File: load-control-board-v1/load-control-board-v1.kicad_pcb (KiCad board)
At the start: 4 copper layers, 100 x 80 mm, 79 parts, among them CN1 3511232BMRS0BNA2, Q1 AO3400A, Q2 AO3400A, Q3 IRFP7530PBF, U1 LM317_SOT-223, U10 OPA188xxDBV, U11 OPA188xxDBV, U12 INA186A1IDCKR, U2 74AHC1G04, U22 TL081HIDBVR, U22 TL081HIDR, U3 LM317_SOT-223, U4 TT56145145-1520, U5 REF5025AD, U6 SN74LVC1G123DCUR_C352969, U7 TL081HIDBVR, U8 OPA188xxDBV, U9 TT56145145-1520

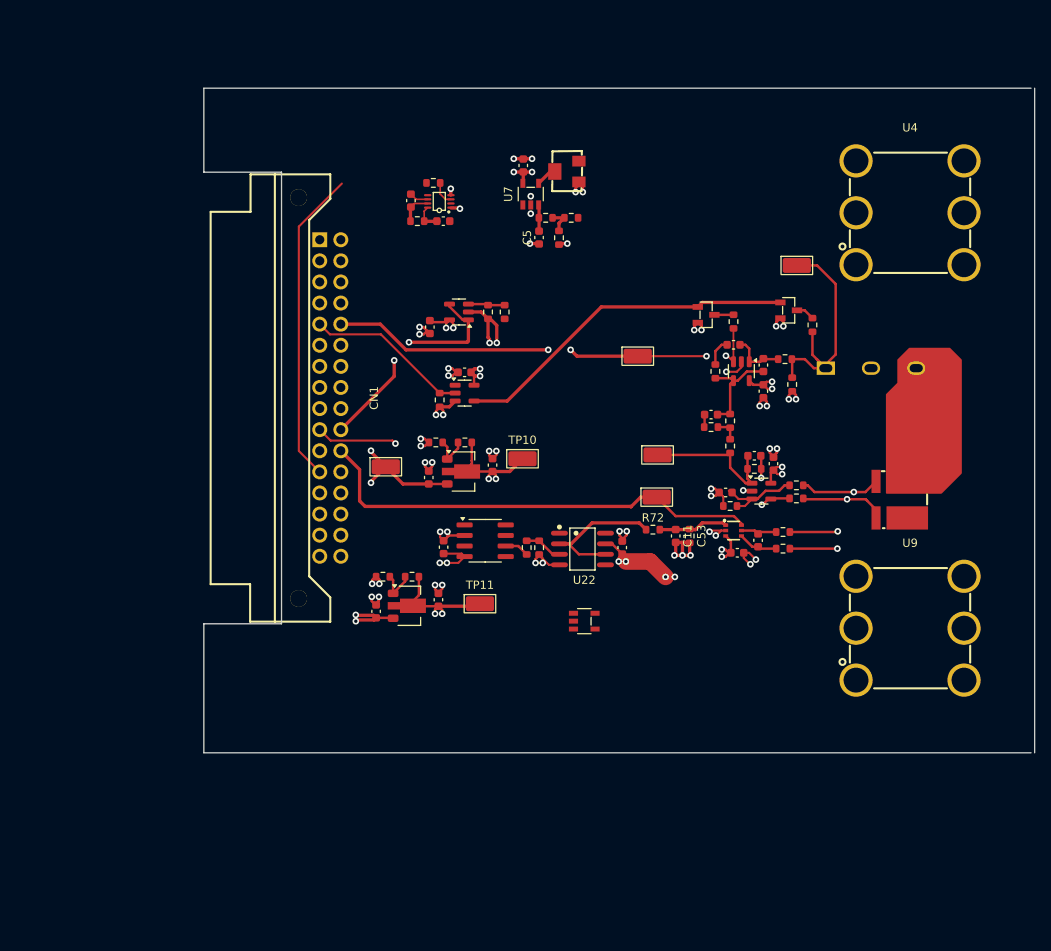
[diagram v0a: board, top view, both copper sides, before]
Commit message: Change layout of LDO and VBUS monitor
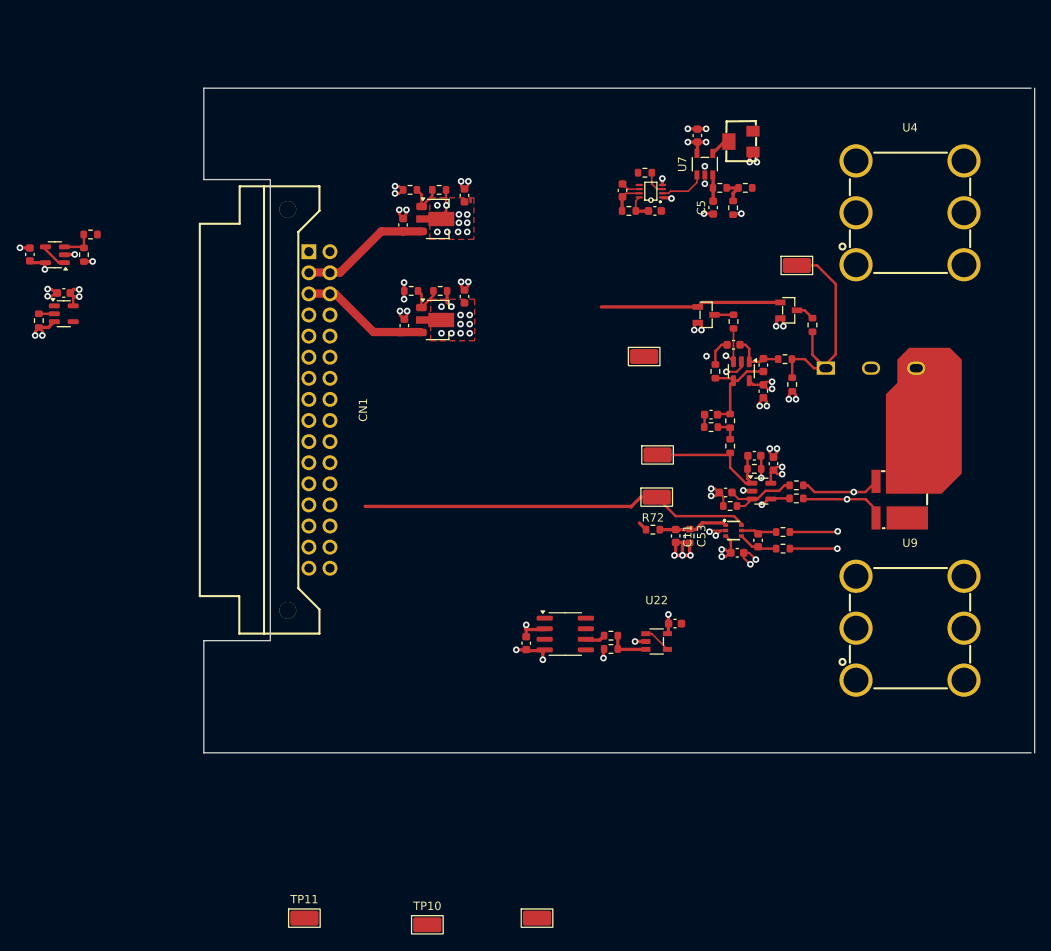
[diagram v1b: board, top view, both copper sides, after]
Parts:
- removed the U22 at (99.8, 109.3)
- moved TP1 57.3 mm to (94.4, 153.7)
- moved TP10 57.3 mm to (81.2, 154.5)
- moved R14 50.7 mm to (40.6, 71.4), turned to 180 degrees
- moved C2 49.2 mm to (37.4, 78.4)
- moved R1 49.2 mm to (34.4, 81.8)
- moved U2 49.2 mm to (37.4, 80.9)
- moved R15 49.1 mm to (39.8, 73.8)
- moved U8 49.1 mm to (36.3, 73.8)
- moved C12 48.9 mm to (33.3, 73.8), turned to -90 degrees
- moved TP11 43.3 mm to (66.4, 153.7)
- moved C6 36.6 mm to (85.6, 78.9)
- moved R6 34.6 mm to (82.7, 78.2)
- moved R7 34.6 mm to (79.2, 78.2)
- moved U3 34.6 mm to (82.4, 81.7)
- moved C4 34.6 mm to (78.4, 82.4)
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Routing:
- net I_CONTROL: track 53.3 -> 7.58 mm, vias 4 -> 2
- net OV_ALERT: track 37.9 -> 0.00 mm
- net +5V: track 69.3 -> 31.6 mm, vias 17 -> 19
- net V_BUS_MON: track 26.9 -> 3.24 mm, vias 2 -> 0
- net ~{ENABLE}: track 41.8 -> 21.8 mm
- net ENABLE: track 19.7 -> 1.86 mm
- net GND: track 86.6 -> 72.0 mm, vias 57 -> 54
- net +9V: track 27.0 -> 12.5 mm, vias 6 -> 14
- net V_REF: track 17.9 -> 4.54 mm
- net +12V: track 20.8 -> 30.9 mm, vias 4 -> 0
- net /I_SINK_MON_CH0: track 55.2 -> 47.3 mm
- net Net-(U6-B): track 0.00 -> 5.58 mm
- net Net-(U5-Vout): track 2.95 -> 2.42 mm
- added copper zone on F.Cu, net +9V
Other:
- outline, holes or cut-outs redrawn

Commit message: Add filled zone for mosfet, change terminal to from THO to SMT
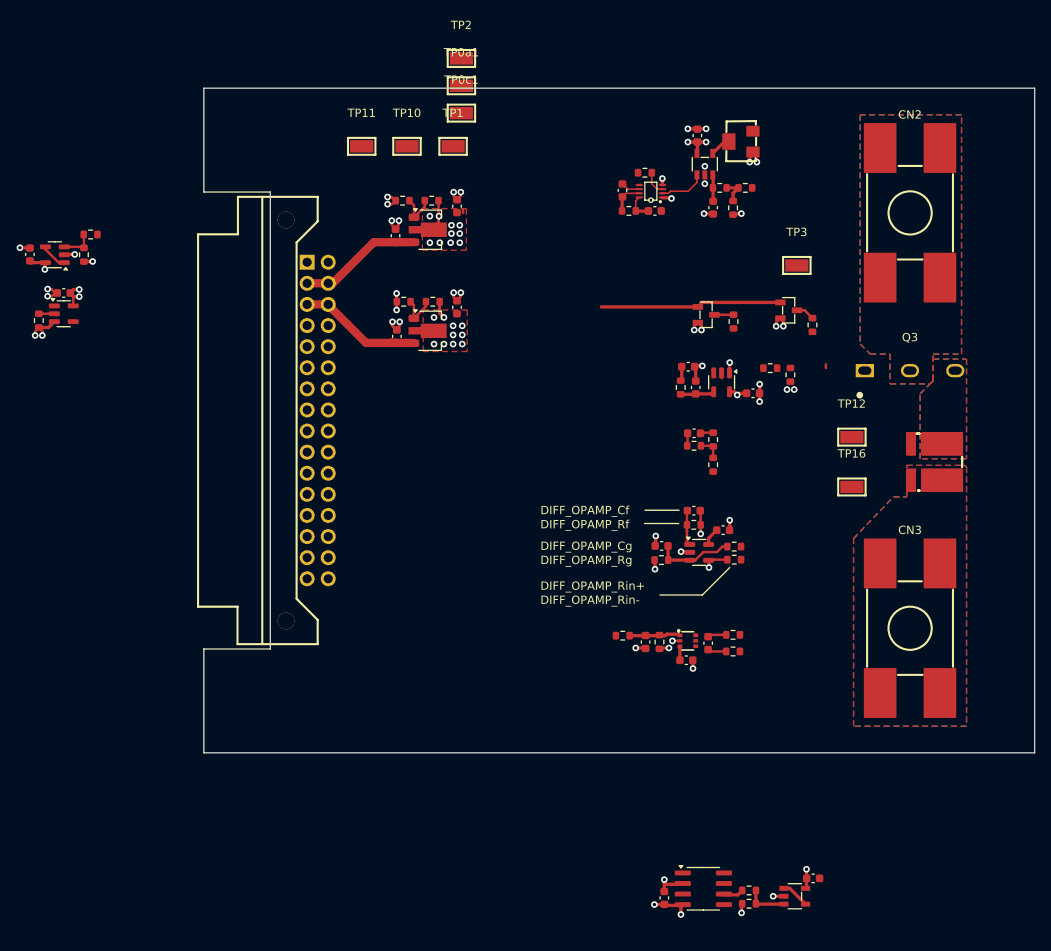
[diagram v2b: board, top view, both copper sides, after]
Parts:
- removed U4, U9: TT56145145-1520, programmable-load-library:TH_6P-TT56145145-1500
- added CN2: BTC22M4NBB4SCM, programmable-load-library:CONN-SMD_L10.8-W10.0-LS17.4, F.Cu at (139.3, 68.8)
- added CN3: BTC22M4NBB4SCM, programmable-load-library:CONN-SMD_L10.8-W10.0-LS17.4, F.Cu at (139.3, 118.8)
- added R_SHUNT1: BVB-M-R001-1.0, programmable-load-library:RES-SMD_4P-L6.9-W6.6_SBB-K-2F-N-T5, F.Cu at (141.3, 98.8)
- added TP12: V_SHUNT_P, programmable-load-library:SMD_RH-5015, F.Cu at (132.3, 95.8)
- added TP16: V_SHUNT_N, programmable-load-library:SMD_RH-5015, F.Cu at (132.3, 101.8)
- Q3: footprint programmable-load-library:PG-TO247-3_L15.9-W5.2-P5.44-L -> programmable-load-library:PG-TO247-3_L15.9-W5.2-P5.44-L_1_Horizontal; moved to F.Cu
- TP0a1: value TestPoint -> I_SINK_MON; footprint TestPoint:TestPoint_Keystone_5015_Micro_Mini -> programmable-load-library:SMD_RH-5015
- TP0c1: value TestPoint -> I_CONTROL_IN; footprint TestPoint:TestPoint_Keystone_5015_Micro_Mini -> programmable-load-library:SMD_RH-5015
- TP1, TP10, TP11: footprint TestPoint:TestPoint_Keystone_5015_Micro_Mini -> programmable-load-library:SMD_RH-5015
- TP2: value TestPoint -> DIFF_OUT; footprint TestPoint:TestPoint_Keystone_5015_Micro_Mini -> programmable-load-library:SMD_RH-5015
- TP3: value TestPoint -> MOS_G; footprint TestPoint:TestPoint_Keystone_5015_Micro_Mini -> programmable-load-library:SMD_RH-5015
- moved TP10 93.7 mm to (78.7, 60.8)
- moved TP1 93.4 mm to (84.3, 60.8)
- moved TP11 93.2 mm to (73.3, 60.8)
- moved TP0a1 54.8 mm to (85.3, 53.5)
- moved TP2 53.2 mm to (85.3, 50.2)
- moved TP0c1 36.6 mm to (85.3, 56.8)
- moved C49 34.9 mm to (127.6, 148.9)
- moved C8 34.9 mm to (109.7, 151.3)
- moved R11 34.9 mm to (119.9, 150.4)
- moved U5 34.9 mm to (114.4, 150.2)
- moved R12 34.9 mm to (119.9, 152.0)
- moved U22 34.9 mm to (125.4, 151.1)
- moved U12 14.4 mm to (112.5, 120.3)
- moved C21 14.3 mm to (112.3, 122.7)
- moved C20 13.8 mm to (115.0, 120.6)
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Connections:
- R_SHUNT1 pad 2: GND -> GNDPWR
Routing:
- net /I_SINK_MON_CH0: track 47.3 -> 0.18 mm
- net /ch0/MOS_G: track 29.6 -> 0.47 mm
- net /ch0/V_Rs0p: track 23.1 -> 0.07 mm, vias 2 -> 0
- net /ch0/V_Rs0n: track 20.5 -> 0.00 mm, vias 2 -> 0
- net GND: track 72.0 -> 54.5 mm, vias 54 -> 49
- net Net-(C15-Pad1): track 17.6 -> 4.17 mm
- net I_CONTROL: track 7.58 -> 0.01 mm, vias 2 -> 0
- net Net-(U11--): track 12.1 -> 5.65 mm
- net Net-(U10--): track 6.40 -> 10.7 mm
- net +9V: track 12.5 -> 8.42 mm, vias 14 -> 11
- net +5V: track 31.6 -> 28.8 mm, vias 19 -> 17
- net Net-(U12-IN+): track 4.81 -> 2.27 mm
- net /ch0/V_REF_FIL: track 8.38 -> 6.19 mm
- net Net-(U12-IN-): track 4.43 -> 2.27 mm
- net Net-(U10-+): track 10.1 -> 8.53 mm
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- added copper zone on F.Cu, net +5V
- added copper zone on B.Cu, net GNDPWR
- added copper zone on F.Cu, net GNDPWR
- added copper zone on B.Cu, net Net-(Q3-S)
- added copper zone on F.Cu, net Net-(Q3-S)
- added copper zone on B.Cu, net VBUS
- added copper zone on F.Cu, net VBUS
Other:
- outline, holes or cut-outs redrawn
- board text added: "0.25V Reference voltage block"
- board text added: "DIFF_OPAMP_Cf"
- board text added: "DIFF_OPAMP_Cg"
- board text added: "DIFF_OPAMP_Rf"
- board text added: "DIFF_OPAMP_Rg"
- board text added: "DIFF_OPAMP_Rin+"
- board text added: "DIFF_OPAMP_Rin-"
- board text added: "INA186 shunt voltage amp & Reference LPF"
- board text added: "Negative feedback Op-Amp"
- board text added: "Shunt voltage DIfferential Op-Amp"

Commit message: Complete second times layout (no copper filled)
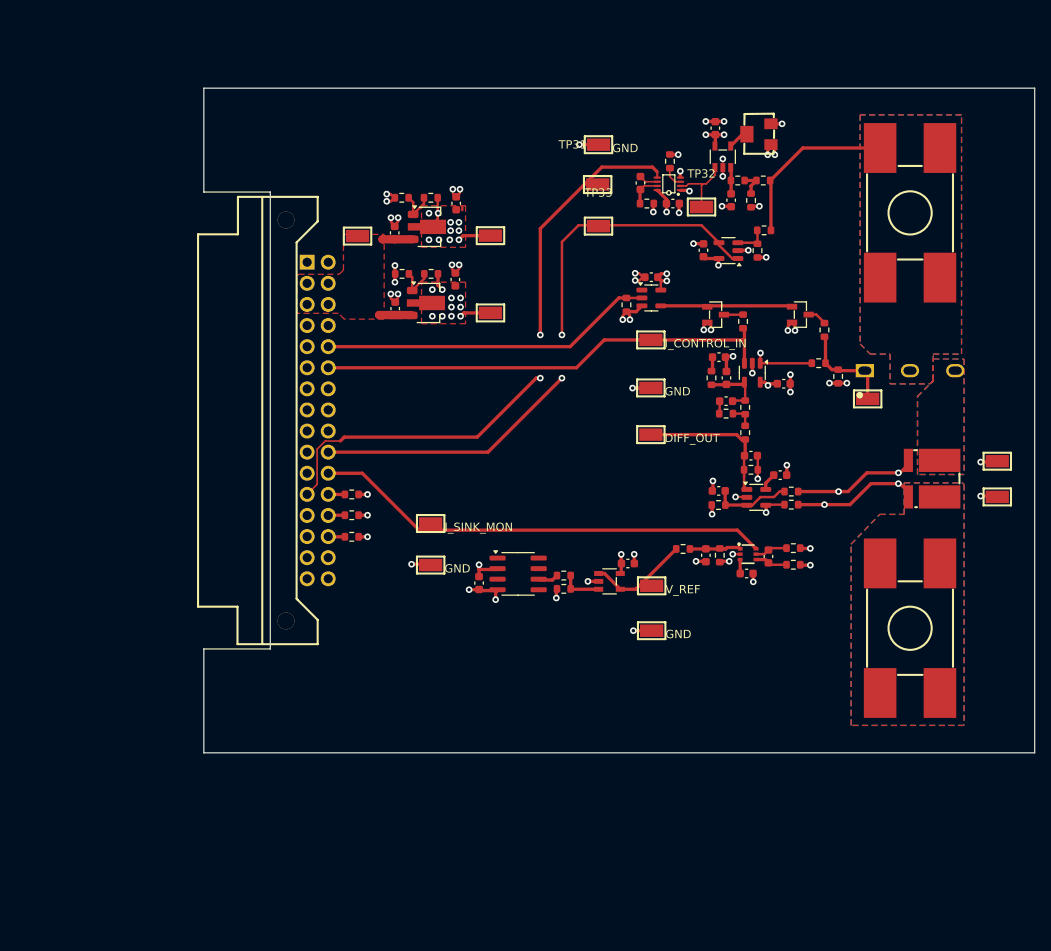
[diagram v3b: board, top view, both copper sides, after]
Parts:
- removed the R_SHUNT1 at (141.3, 98.8) (x2)
- added R76: 10k, Resistor_SMD:R_0603_1608Metric, F.Cu at (72.1, 102.7)
- added R77: 10k, Resistor_SMD:R_0603_1608Metric, F.Cu at (72.1, 105.2)
- added R78: 10k, Resistor_SMD:R_0603_1608Metric, F.Cu at (72.1, 107.8)
- added R_SHUNT1: BVB-M-R001-1.0, programmable-load-library:RES-SMD_4P-L6.9-W6.6_SBB-K-2F-N-T5, F.Cu at (140.9, 100.8)
- added TP20: GND, programmable-load-library:SMD_RH-5015, F.Cu at (101.8, 60.6)
- added TP21: GND, programmable-load-library:SMD_RH-5015, F.Cu at (108.2, 119.1)
- added TP22: GND, programmable-load-library:SMD_RH-5015, F.Cu at (81.6, 111.2)
- added TP26: GND, programmable-load-library:SMD_RH-5015, F.Cu at (108.1, 89.9)
- added TP30: REF, programmable-load-library:SMD_RH-5015, F.Cu at (108.2, 113.7)
- added TP31: V_BUS_MON, programmable-load-library:SMD_RH-5015, F.Cu at (101.7, 65.4)
- added TP32: VBUS_COMP_OUT, programmable-load-library:SMD_RH-5015, F.Cu at (114.2, 68.1)
- added TP33: OV_ALERT, programmable-load-library:SMD_RH-5015, F.Cu at (101.8, 70.4)
- U7: value TL081HIDBVR -> ALERT_COMP_OUT
- moved C12 81.1 mm to (114.4, 73.3)
- moved R14 81.1 mm to (121.7, 70.9)
- moved R15 81.1 mm to (120.9, 73.3)
- moved U8 81.1 mm to (117.4, 73.3)
- moved C2 70.8 mm to (108.1, 76.5)
- moved R1 70.8 mm to (105.1, 79.9)
- moved U2 70.8 mm to (108.1, 79.0)
- moved TP0a1 52.8 mm to (81.6, 106.2)
- moved TP2 50.7 mm to (108.1, 95.5)
- moved C49 44.0 mm to (105.3, 111.0)
- moved C8 44.0 mm to (87.4, 113.4)
- moved R11 44.0 mm to (97.6, 112.5)
- moved U5 44.0 mm to (92.1, 112.3)
- moved R12 44.0 mm to (97.6, 114.1)
- moved U22 44.0 mm to (103.1, 113.2)
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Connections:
- CN1 pad 21: I_CONTROL -> ENABLE
- CN1 pad 22: unconnected-(CN1-B6-Pad22) -> I_CONTROL
- CN1 pad 5: ENABLE -> unconnected-(CN1-A5-Pad5)
- R10 pad 1: 5V -> +5V
- R9 pad 3: 5V -> +5V
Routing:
- net OV_ALERT: track 0.00 -> 72.4 mm, vias 0 -> 2
- net V_BUS_MON: track 3.24 -> 72.1 mm, vias 0 -> 2
- net I_CONTROL: track 0.01 -> 55.8 mm
- net /I_SINK_MON_CH0: track 0.18 -> 55.4 mm
- net /ch0/V_Rs0p: track 0.07 -> 39.1 mm, vias 0 -> 4
- net ENABLE: track 1.86 -> 40.2 mm
- net /ch0/V_Rs0n: track 0.00 -> 35.1 mm, vias 0 -> 4
- net +12V: track 30.9 -> 9.39 mm
- net VBUS: track 0.00 -> 20.9 mm
- net GND: track 54.5 -> 74.4 mm, vias 49 -> 59
- net Net-(C15-Pad1): track 4.17 -> 17.8 mm
- net /ch0/MOS_G: track 0.47 -> 11.9 mm
- net V_REF: track 3.39 -> 12.1 mm
- net +5V: track 28.8 -> 36.2 mm, vias 17 -> 21
- net Net-(C18-Pad1): track 7.71 -> 13.9 mm
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- added copper zone on F.Cu, net +12V
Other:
- board text added: "DIFF_OUT"
- board text added: "GND"
- board text added: "I_CONTROL_IN"
- board text added: "I_SINK_MON"
- board text added: "V_REF"

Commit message: connection and drc check
connection of power layer is done
drc checked
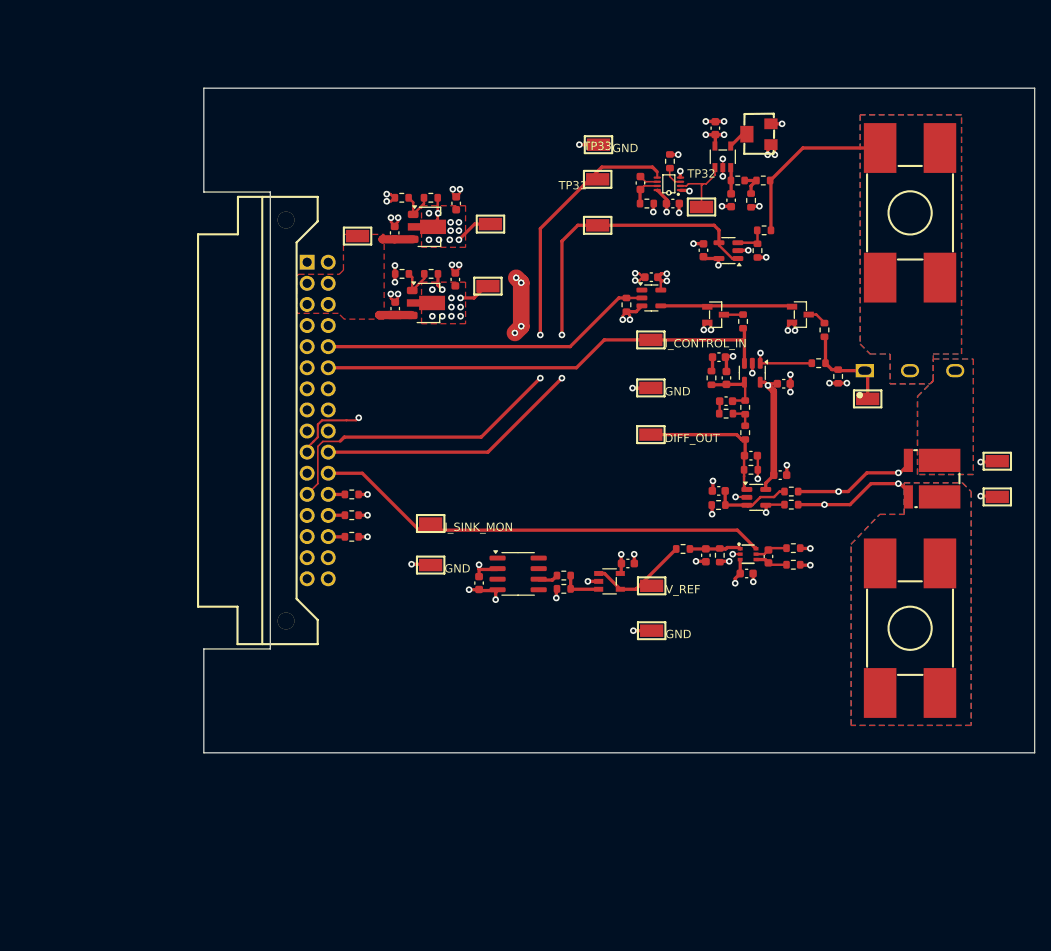
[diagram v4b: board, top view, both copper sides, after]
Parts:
- moved TP33 5.63 mm to (101.7, 64.8)
- moved TP31 4.91 mm to (101.7, 70.3)
- moved TP11 3.24 mm to (88.4, 77.6)
- moved TP10 1.39 mm to (88.8, 70.2)
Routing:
- net +5V: track 36.2 -> 234.2 mm, vias 21 -> 27
- net +9V: track 12.2 -> 65.5 mm
- net V_BUS_MON: track 72.1 -> 73.0 mm
- added copper zone on In1.Cu, net GND
